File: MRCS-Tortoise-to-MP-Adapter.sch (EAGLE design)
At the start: 6 parts, among them K1 G6H2-100

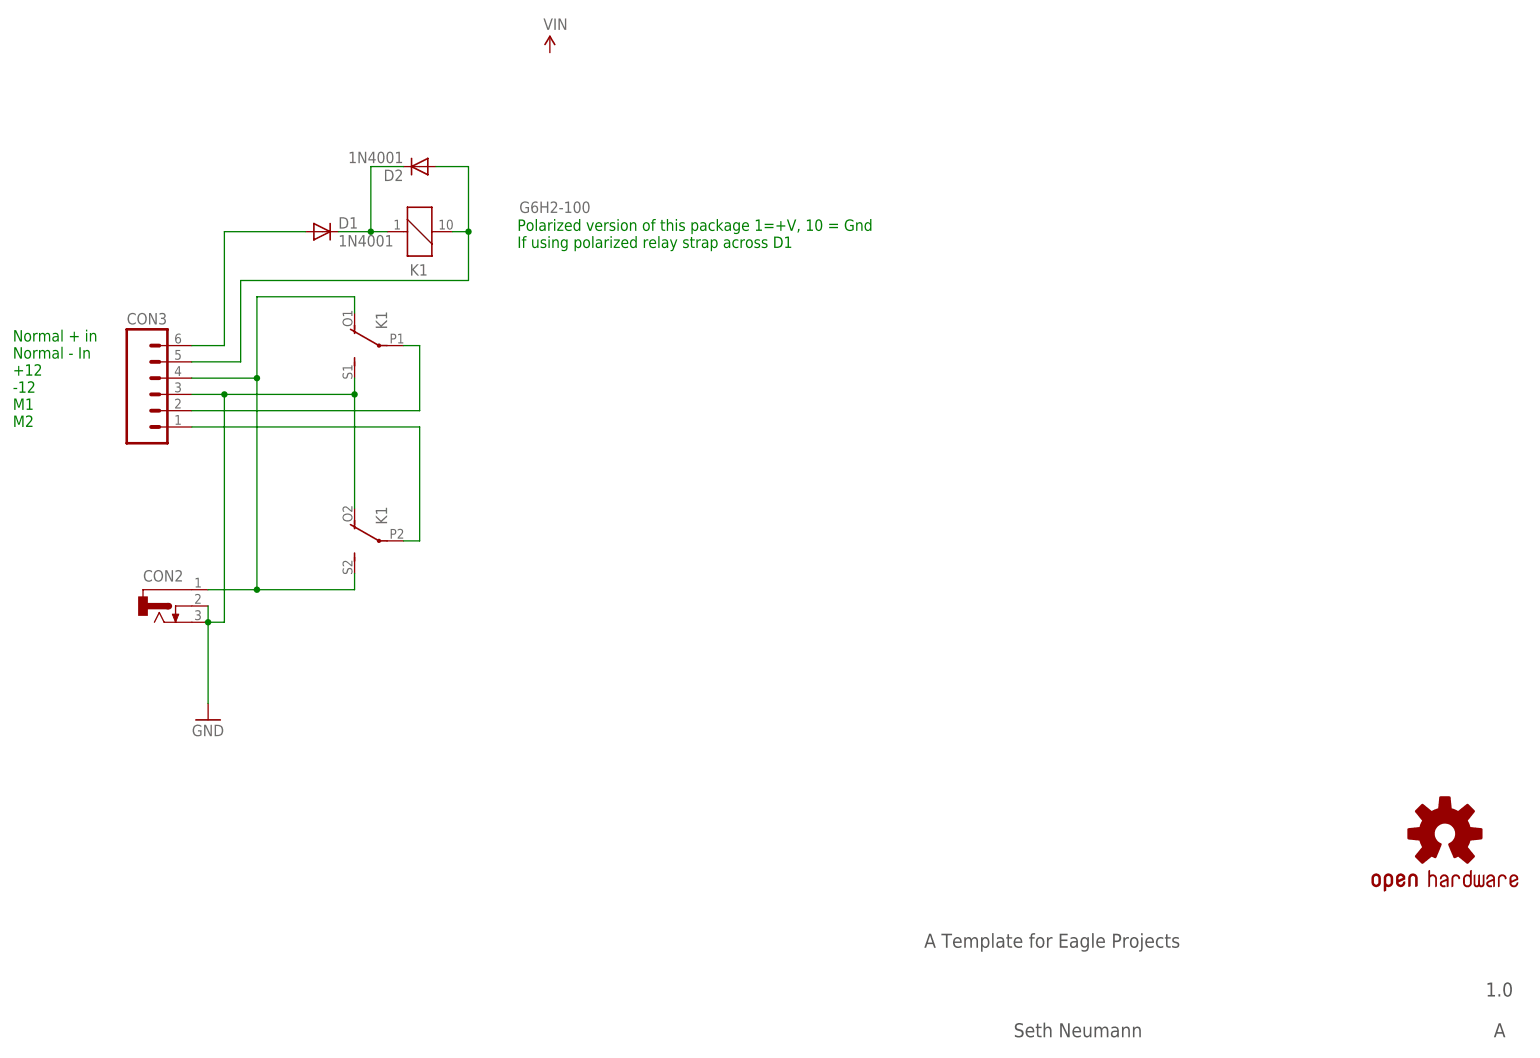
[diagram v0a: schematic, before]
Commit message: clean up in preparation for panelization
1st rev worked well and seems OK, add Prop 65 warning and minor label cleanup
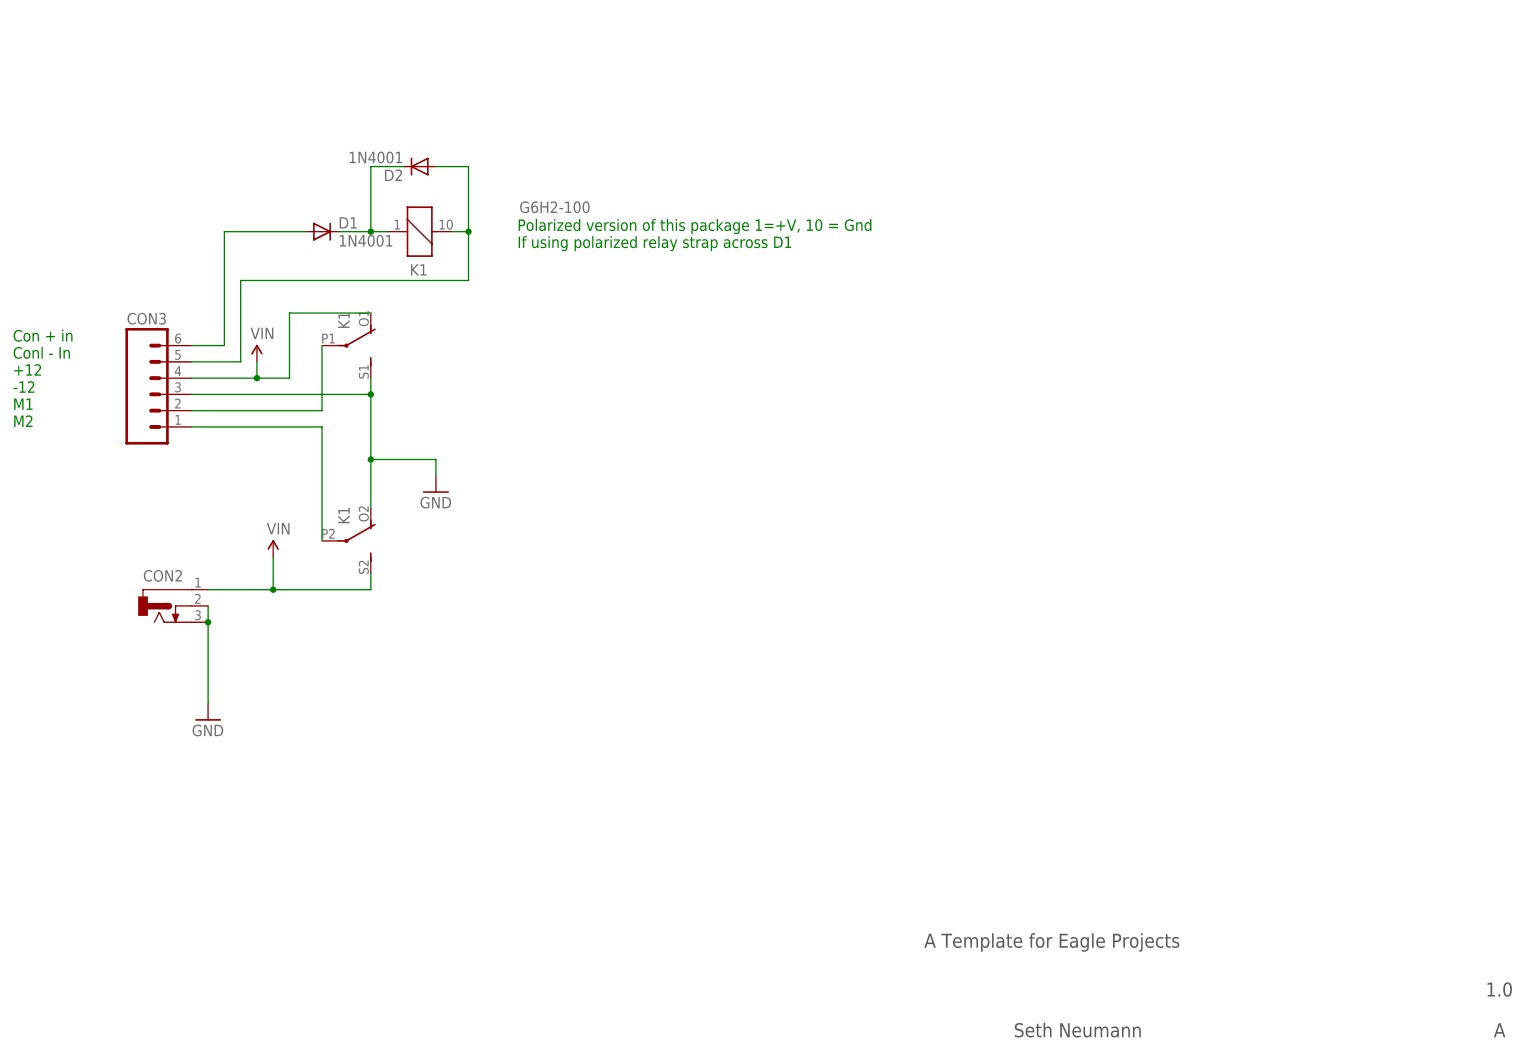
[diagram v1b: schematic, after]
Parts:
- removed OSHW1: DOC-OSHW-LOGO-M, SPCoast:DOC-OSHW-LOGO-M
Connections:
- net N$4 renamed VIN
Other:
- note added: "Con + in Conl - In +12 -12 M1 M2"
- note removed: "Normal + in Normal - In +12 -12 M1 M2"
- moved on the sheet: K1
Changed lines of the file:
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@@
 <parts>
 <part name="FRAME1" library="SPCoast" deviceset="DOC-FRAME-LETTER" device=""/>
-<part name="OSHW1" library="SPCoast" deviceset="DOC-OSHW-LOGO-" device="M"/>
 <part name="K1" library="relay" deviceset="G6H2-100" device=""/>
 <part name="D1" library="SPCoast" deviceset="DIODE" device="PTH" value="1N4001"/>
@@
 <part name="D2" library="SPCoast" deviceset="DIODE" device="PTH" value="1N4001"/>
 <part name="GND1" library="SPCoast" deviceset="GND" device=""/>
+<part name="SUPPLY2" library="SparkFun-Aesthetics" deviceset="VIN" device=""/>
+<part name="GND2" library="SPCoast" deviceset="GND" device=""/>
 </parts>
 <sheets>
@@
 <text x="88.9" y="129.54" size="1.778" layer="91">Polarized version of this package 1=+V, 10 = Gnd
 If using polarized relay strap across D1</text>
-<text x="10.16" y="101.6" size="1.778" layer="91">Normal + in
-Normal - In
+<text x="10.16" y="101.6" size="1.778" layer="91">Con + in
+Conl - In
 +12
 -12
@@
 <instance part="FRAME1" gate="FRAME" x="0" y="0"/>
 <instance part="FRAME1" gate="FRAME_CONTENT" x="147.32" y="0"/>
-<instance part="OSHW1" gate="DOC-OSHW-LOGO" x="233.68" y="38.1"/>
 <instance part="K1" gate="1" x="73.66" y="132.08" smashed="yes" rot="R90">
 <attribute name="VALUE" x="100.33" y="136.779" size="1.778" layer="96" rot="R180"/>
 <attribute name="PART" x="74.93" y="127" size="1.778" layer="95" rot="R180"/>
 </instance>
-<instance part="K1" gate="2" x="68.58" y="114.3" rot="R90"/>
-<instance part="K1" gate="3" x="68.58" y="83.82" rot="R90"/>
+<instance part="K1" gate="2" x="60.96" y="114.3" rot="MR90"/>
+<instance part="K1" gate="3" x="60.96" y="83.82" rot="MR90"/>
 <instance part="D1" gate="D1" x="58.42" y="132.08"/>
 <instance part="CON2" gate="J" x="33.02" y="73.66"/>
-<instance part="SUPPLY1" gate="G$1" x="93.98" y="160.02"/>
+<instance part="SUPPLY1" gate="G$1" x="48.26" y="111.76"/>
 <instance part="CON3" gate="J" x="33.02" y="106.68"/>
 <instance part="D2" gate="D1" x="73.66" y="142.24" rot="R180"/>
 <instance part="GND1" gate="1" x="40.64" y="55.88"/>
+<instance part="SUPPLY2" gate="G$1" x="50.8" y="81.28"/>
+<instance part="GND2" gate="1" x="76.2" y="91.44"/>
 </instances>
 <busses>
@@
 </segment>
 </net>
-<net name="N$4" class="0">
-<segment>
-<pinref part="CON3" gate="J" pin="4"/>
-<wire x1="38.1" y1="109.22" x2="48.26" y2="109.22" width="0.4064" layer="91"/>
-<wire x1="48.26" y1="109.22" x2="48.26" y2="121.92" width="0.4064" layer="91"/>
-<wire x1="48.26" y1="121.92" x2="63.5" y2="121.92" width="0.4064" layer="91"/>
-<pinref part="K1" gate="2" pin="O"/>
-<wire x1="63.5" y1="121.92" x2="63.5" y2="119.38" width="0.4064" layer="91"/>
-<wire x1="48.26" y1="109.22" x2="48.26" y2="76.2" width="0.4064" layer="91"/>
-<wire x1="48.26" y1="76.2" x2="63.5" y2="76.2" width="0.4064" layer="91"/>
-<pinref part="K1" gate="3" pin="S"/>
-<wire x1="63.5" y1="76.2" x2="63.5" y2="78.74" width="0.4064" layer="91"/>
-<junction x="48.26" y="109.22"/>
-<pinref part="CON2" gate="J" pin="1"/>
-<wire x1="48.26" y1="76.2" x2="40.64" y2="76.2" width="0.4064" layer="91"/>
-<junction x="48.26" y="76.2"/>
-</segment>
-</net>
 <net name="N$6" class="0">
 <segment>
 <pinref part="CON3" gate="J" pin="2"/>
-<wire x1="38.1" y1="104.14" x2="73.66" y2="104.14" width="0.4064" layer="91"/>
-<wire x1="73.66" y1="104.14" x2="73.66" y2="114.3" width="0.4064" layer="91"/>
+<wire x1="38.1" y1="104.14" x2="58.42" y2="104.14" width="0.4064" layer="91"/>
+<wire x1="58.42" y1="104.14" x2="58.42" y2="114.3" width="0.4064" layer="91"/>
 <pinref part="K1" gate="2" pin="P"/>
-<wire x1="73.66" y1="114.3" x2="71.12" y2="114.3" width="0.4064" layer="91"/>
 </segment>
 </net>
@@
 <segment>
 <pinref part="CON3" gate="J" pin="1"/>
-<wire x1="38.1" y1="101.6" x2="73.66" y2="101.6" width="0.4064" layer="91"/>
-<wire x1="73.66" y1="101.6" x2="73.66" y2="83.82" width="0.4064" layer="91"/>
+<wire x1="38.1" y1="101.6" x2="58.42" y2="101.6" width="0.4064" layer="91"/>
+<wire x1="58.42" y1="101.6" x2="58.42" y2="83.82" width="0.4064" layer="91"/>
 <pinref part="K1" gate="3" pin="P"/>
-<wire x1="73.66" y1="83.82" x2="71.12" y2="83.82" width="0.4064" layer="91"/>
 </segment>
 </net>
 <net name="GND" class="0">
 <segment>
+<pinref part="GND1" gate="1" pin="GND"/>
 <pinref part="CON2" gate="J" pin="2"/>
-<pinref part="GND1" gate="1" pin="GND"/>
 <wire x1="40.64" y1="73.66" x2="40.64" y2="71.12" width="0.4064" layer="91"/>
 <pinref part="CON2" gate="J" pin="3"/>
 <junction x="40.64" y="71.12"/>
 <wire x1="40.64" y1="71.12" x2="40.64" y2="58.42" width="0.4064" layer="91"/>
+</segment>
+<segment>
+<pinref part="GND2" gate="1" pin="GND"/>
+<wire x1="76.2" y1="93.98" x2="76.2" y2="96.52" width="0.4064" layer="91"/>
 <pinref part="CON3" gate="J" pin="3"/>
+<wire x1="38.1" y1="106.68" x2="66.04" y2="106.68" width="0.4064" layer="91"/>
+<pinref part="K1" gate="3" pin="O"/>
+<wire x1="66.04" y1="106.68" x2="66.04" y2="96.52" width="0.4064" layer="91"/>
+<wire x1="66.04" y1="96.52" x2="66.04" y2="88.9" width="0.4064" layer="91"/>
+<wire x1="76.2" y1="96.52" x2="66.04" y2="96.52" width="0.4064" layer="91"/>
+<junction x="66.04" y="96.52"/>
 <pinref part="K1" gate="2" pin="S"/>
-<wire x1="38.1" y1="106.68" x2="43.18" y2="106.68" width="0.4064" layer="91"/>
-<wire x1="43.18" y1="106.68" x2="63.5" y2="106.68" width="0.4064" layer="91"/>
-<wire x1="63.5" y1="106.68" x2="63.5" y2="109.22" width="0.4064" layer="91"/>
-<pinref part="K1" gate="3" pin="O"/>
-<wire x1="63.5" y1="106.68" x2="63.5" y2="88.9" width="0.4064" layer="91"/>
-<junction x="63.5" y="106.68"/>
-<wire x1="43.18" y1="106.68" x2="43.18" y2="71.12" width="0.4064" layer="91"/>
-<wire x1="43.18" y1="71.12" x2="40.64" y2="71.12" width="0.4064" layer="91"/>
-<junction x="43.18" y="106.68"/>
+<wire x1="66.04" y1="106.68" x2="66.04" y2="109.22" width="0.4064" layer="91"/>
+<junction x="66.04" y="106.68"/>
 </segment>
 </net>
+<net name="VIN" class="0">
+<segment>
+<pinref part="SUPPLY1" gate="G$1" pin="VIN"/>
+<wire x1="48.26" y1="109.22" x2="48.26" y2="111.76" width="0.4064" layer="91"/>
+<wire x1="53.34" y1="109.22" x2="48.26" y2="109.22" width="0.4064" layer="91"/>
+<junction x="48.26" y="109.22"/>
+<pinref part="CON3" gate="J" pin="4"/>
+<wire x1="38.1" y1="109.22" x2="48.26" y2="109.22" width="0.4064" layer="91"/>
+<pinref part="K1" gate="2" pin="O"/>
+<wire x1="66.04" y1="119.38" x2="53.34" y2="119.38" width="0.4064" layer="91"/>
+<wire x1="53.34" y1="119.38" x2="53.34" y2="109.22" width="0.4064" layer="91"/>
+</segment>
+<segment>
+<wire x1="40.64" y1="76.2" x2="50.8" y2="76.2" width="0.4064" layer="91"/>
+<pinref part="K1" gate="3" pin="S"/>
+<wire x1="50.8" y1="76.2" x2="66.04" y2="76.2" width="0.4064" layer="91"/>
+<wire x1="66.04" y1="76.2" x2="66.04" y2="78.74" width="0.4064" layer="91"/>
+<pinref part="CON2" gate="J" pin="1"/>
+<pinref part="SUPPLY2" gate="G$1" pin="VIN"/>
+<wire x1="50.8" y1="81.28" x2="50.8" y2="76.2" width="0.4064" layer="91"/>
+<junction x="50.8" y="76.2"/>
+</segment>
+</net>
